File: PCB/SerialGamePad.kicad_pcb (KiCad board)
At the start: 2 copper layers, 33.5 x 30.7 mm, 13 parts, among them P0 CONN_01X02, P1 CONN_01X02, P2 CONN_01X02, P3 CONN_01X02, P4 CONN_01X02, P5 CONN_01X02

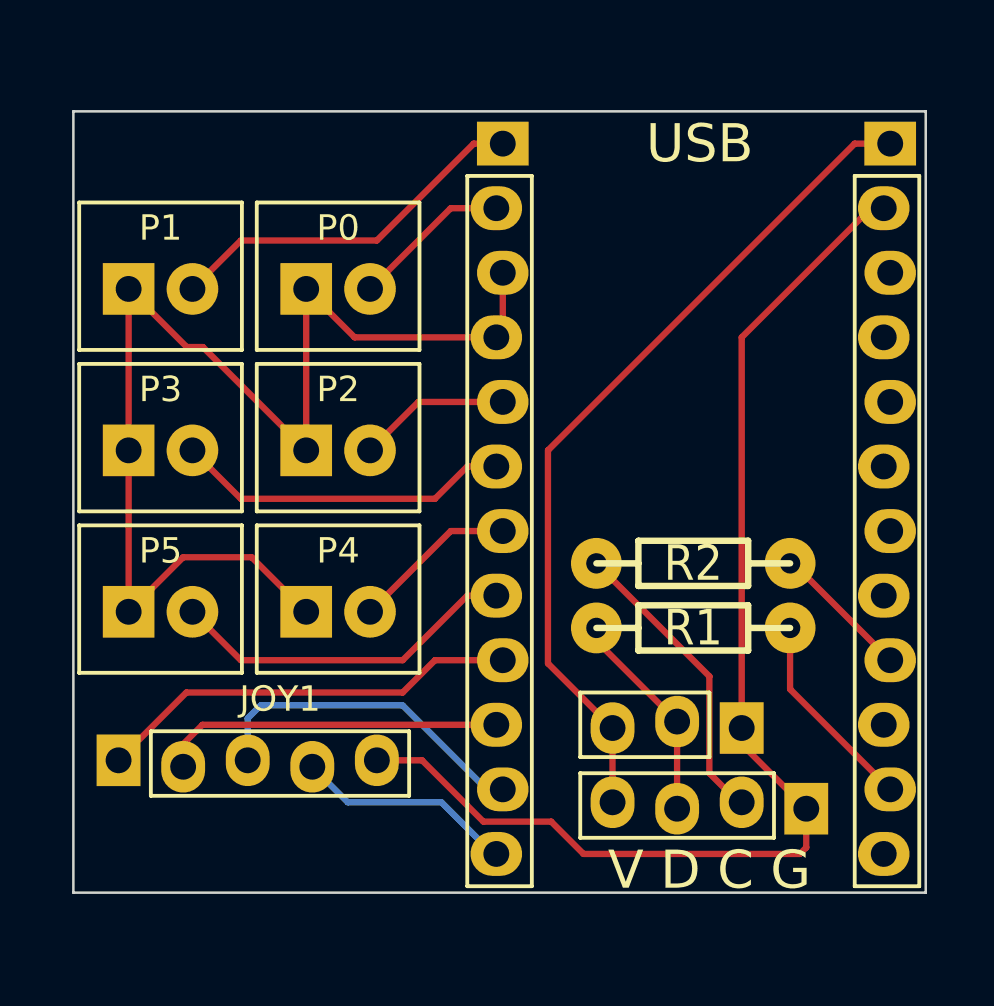
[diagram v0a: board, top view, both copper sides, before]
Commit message: fixing autosaves
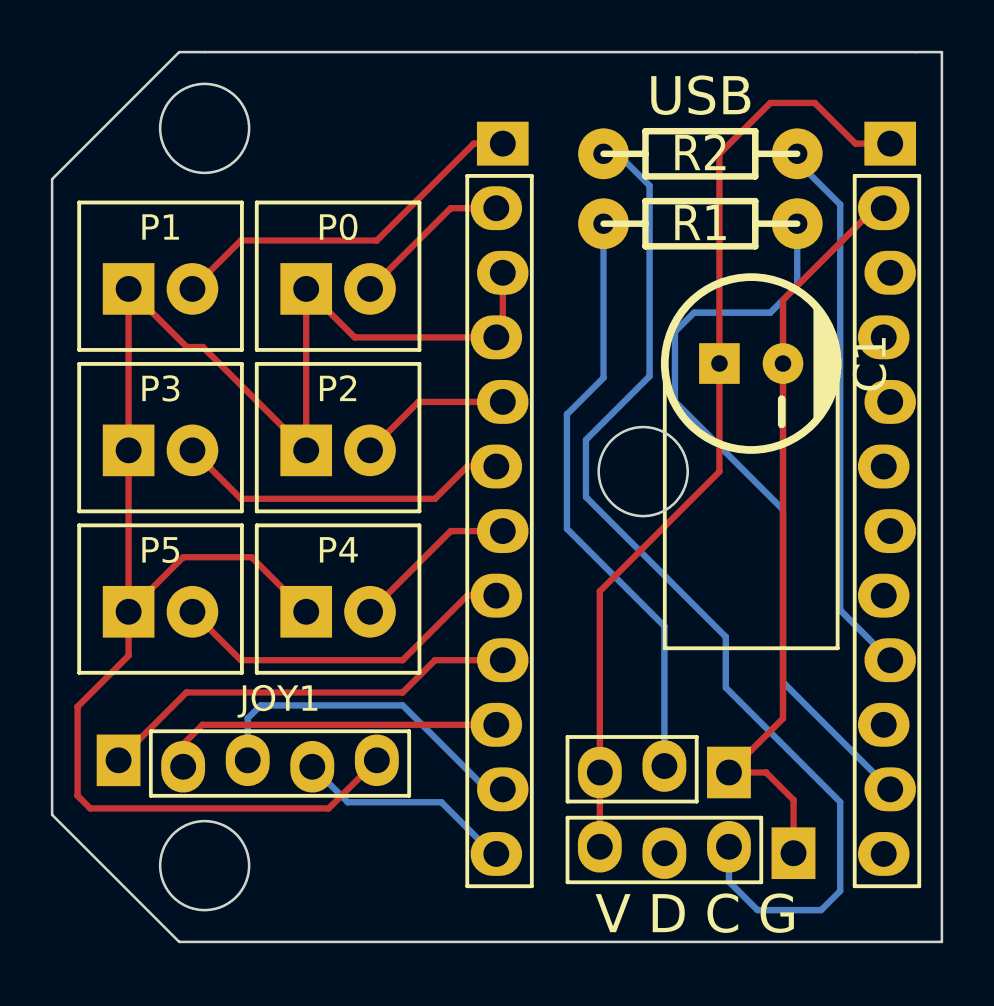
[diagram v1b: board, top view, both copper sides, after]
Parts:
- added C1: CP1, PCB:CP_6.3x11mm_90, F.Cu at (111.5, 110.2)
- moved R2 16.1 mm to (109.5, 102.0)
- moved R1 15.9 mm to (109.5, 104.8)
- moved L1 1.82 mm to (110.6, 126.2)
- moved L2 1.82 mm to (113.2, 129.4)
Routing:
- net Net-(L2-Pad2): track 11.8 -> 41.9 mm
- net MOSI: track 7.98 -> 29.5 mm
- net SCLK: track 5.52 -> 21.4 mm
- net Net-(L1-Pad2): track 8.43 -> 23.5 mm
- net RAW: track 33.4 -> 37.4 mm
- net GND: track 95.7 -> 99.7 mm
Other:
- board size 33.5 x 30.7 mm -> 35 x 35 mm
